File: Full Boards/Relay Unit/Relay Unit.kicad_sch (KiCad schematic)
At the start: 156 parts, among them J3 Program Header, SW1 Status Switch, SW3 SW_MEC_5G, SW4 SW_MEC_5G, U1 ISO1044BD, U10 FM24CL64B-G, U15 LM1117MP-5.0, U2 MAX3232, U3 STM32C092KCT6, U4 ULN2003A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

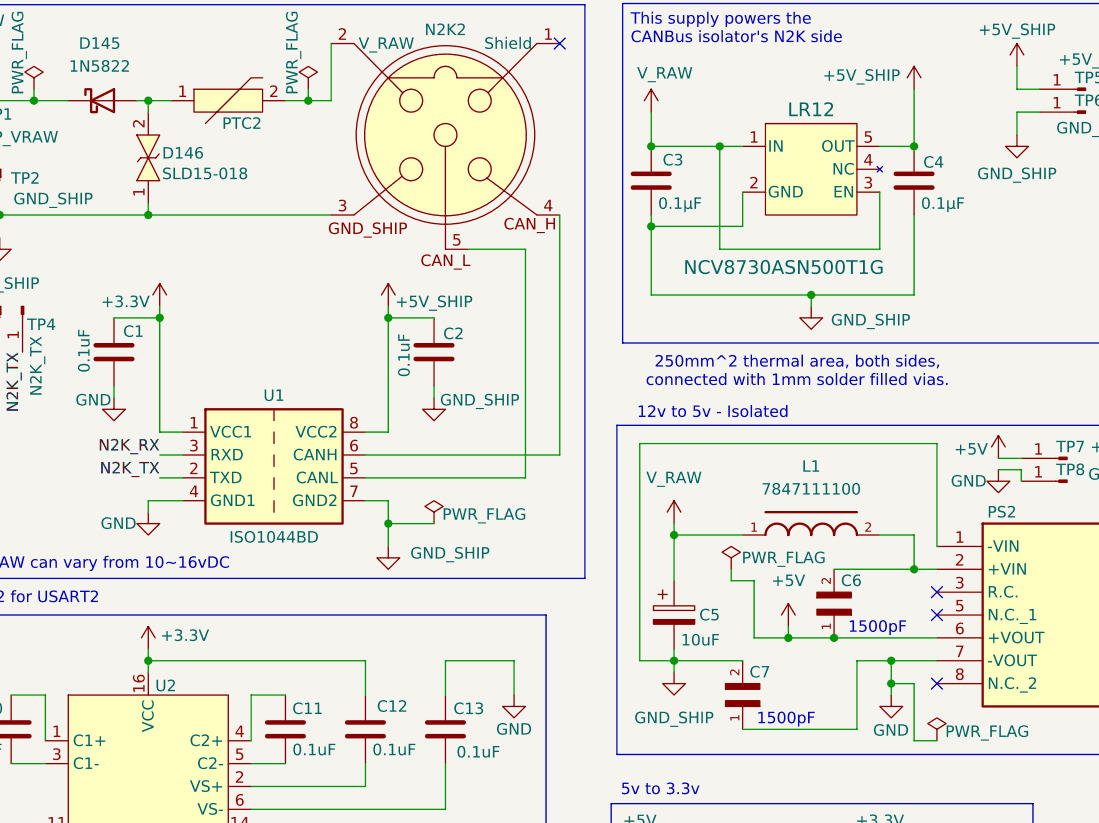
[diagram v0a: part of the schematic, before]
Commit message: Updated PCBs to swap RVS diodes from SLD15-018 to SLD22-018. Also swapped out the inductor from 7847111100 to PA4340.103NLT.
Signed-off-by: Madison Kelly <digital.mermaid@gmail.com>
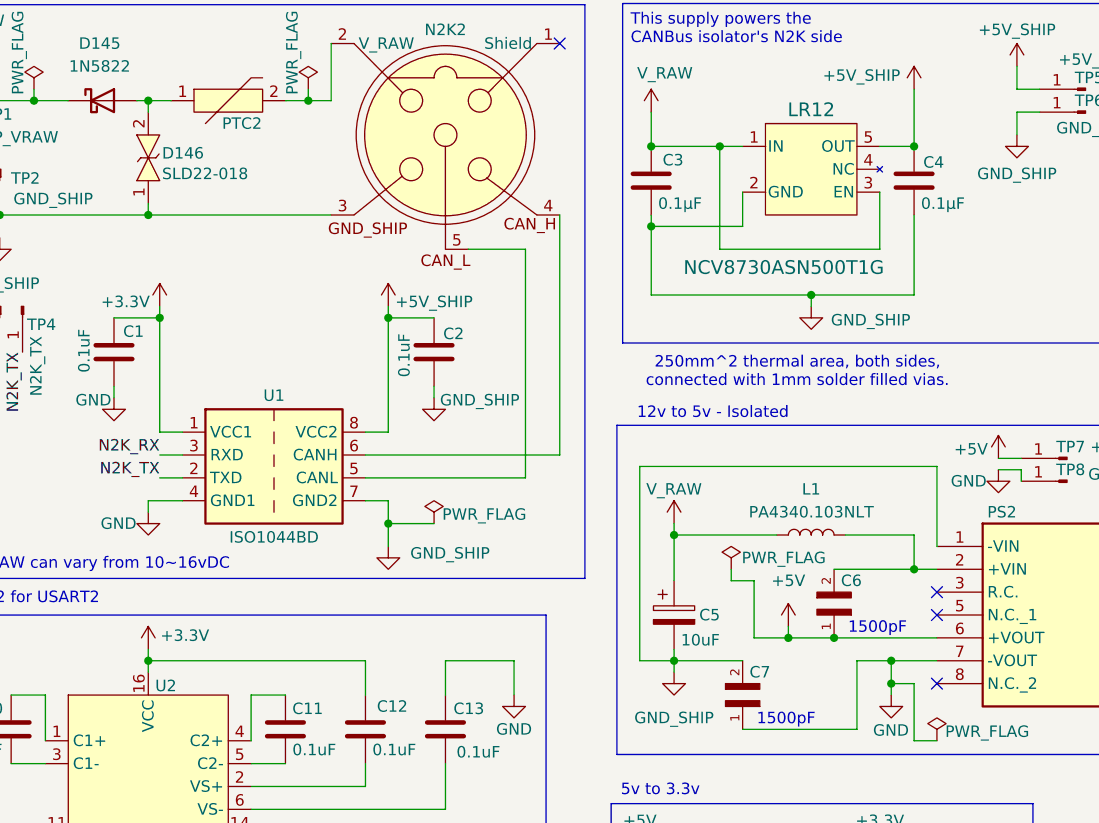
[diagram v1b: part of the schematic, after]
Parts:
- removed L1: 7847111100, mr-stuff:WE-RCIT_7847111100, symbol mr-parts:WE-RCIT
- added L1: PA4340.103NLT, mr-stuff:Pulse PA4340.103NLT, symbol Device:L
- D146: value SLD15-018 -> SLD22-018
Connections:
- net V_RAW: now also L1.1
- net at C6.2, PS2.2 (+VIN): now also L1.2
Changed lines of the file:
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@@
 	(wire
 		(pts
-			(xy 121.92 74.93) (xy 118.11 74.93)
-		)
-		(stroke
-			(width 0)
-			(type default)
-		)
-	)
-	(wire
-		(pts
 			(xy 198.12 224.79) (xy 198.12 227.33)
 		)
@@
 	(wire
 		(pts
-			(xy 91.44 64.77) (xy 91.44 88.9)
+			(xy 91.44 67.31) (xy 91.44 88.9)
 		)
 		(stroke
@@
 	(wire
 		(pts
-			(xy 95.25 74.93) (xy 102.87 74.93)
+			(xy 95.25 74.93) (xy 106.68 74.93)
 		)
 		(stroke
@@
 	(wire
 		(pts
-			(xy 124.46 76.2) (xy 124.46 64.77)
+			(xy 124.46 76.2) (xy 124.46 67.31)
 		)
 		(stroke
@@
 	(wire
 		(pts
-			(xy 124.46 64.77) (xy 91.44 64.77)
+			(xy 124.46 67.31) (xy 91.44 67.31)
 		)
 		(stroke
@@
 	(wire
 		(pts
+			(xy 114.3 74.93) (xy 121.92 74.93)
+		)
+		(stroke
+			(width 0)
+			(type default)
+		)
+	)
+	(wire
+		(pts
 			(xy 124.46 161.29) (xy 132.08 161.29)
 		)
@@
 	)
 	(symbol
+		(lib_id "Device:L")
+		(at 110.49 74.93 90)
+		(unit 1)
+		(exclude_from_sim no)
+		(in_bom yes)
+		(on_board yes)
+		(dnp no)
+		(fields_autoplaced yes)
+		(property "Reference" "L1"
+			(at 110.49 69.85 90)
+			(effects
+				(font
+					(size 1.27 1.27)
+				)
+			)
+		)
+		(property "Value" "PA4340.103NLT"
+			(at 110.49 72.39 90)
+			(effects
+				(font
+					(size 1.27 1.27)
+				)
+			)
+		)
+		(property "Footprint" "mr-stuff:Pulse PA4340.103NLT"
+			(at 110.49 74.93 0)
+			(effects
+				(font
+					(size 1.27 1.27)
+				)
+				(hide yes)
+			)
+		)
+		(property "Datasheet" "~"
+			(at 110.49 74.93 0)
+			(effects
+				(font
+					(size 1.27 1.27)
+				)
+				(hide yes)
+			)
+		)
+		(property "Description" "Inductor"
+			(at 110.49 74.93 0)
+			(effects
+				(font
+					(size 1.27 1.27)
+				)
+				(hide yes)
+			)
+		)
+		(pin "2"
+		)
+		(pin "1"
+		)
+		(instances
+			(project "Relay Unit"
+				(path "/cdf85de7-e063-4a45-8f3b-41b7e4c09bb1"
+					(reference "L1")
+					(unit 1)
+				)
+			)
+		)
+	)
+	(symbol
 		(lib_id "mr-parts:Keystone Electronics 7799")
 		(at 304.8 39.37 0)
@@
 			)
 		)
-		(property "Value" "SLD15-018"
+		(property "Value" "SLD22-018"
 			(at 38.354 34.798 90)
 			(effects
@@
 		(on_board yes)
 		(dnp no)
-		(fields_autoplaced yes)
 		(property "Reference" "#PWR075"
 			(at 95.25 77.47 0)
@@
 		)
 		(property "Value" "V_RAW"
-			(at 95.25 68.58 0)
+			(at 95.25 69.85 0)
 			(effects
 				(font
@@
 					(unit 1)
 				)
-			)
-		)
-	)
-	(symbol
-		(lib_id "mr-parts:WE-RCIT")
-		(at 110.49 74.93 0)
-		(unit 1)
-		(exclude_from_sim no)
-		(in_bom yes)
-		(on_board yes)
-		(dnp no)
-		(fields_autoplaced yes)
-		(property "Reference" "L1"
-			(at 110.49 67.31 0)
-			(effects
-				(font
-					(size 1.27 1.27)
-				)
-			)
-		)
-		(property "Value" "7847111100"
-			(at 110.49 69.85 0)
-			(effects
-				(font
-					(size 1.27 1.27)
-				)
-			)
-		)
-		(property "Footprint" "mr-stuff:WE-RCIT_7847111100"
-			(at 110.744 80.01 0)
-			(effects
-				(font
-					(size 1.27 1.27)
-				)
-				(justify bottom)
-				(hide yes)
-			)
-		)
-		(property "Datasheet" "https://www.we-online.com/components/products/datasheet/7847111100.pdf"
-			(at 110.49 74.93 0)
-			(effects
-				(font
-					(size 1.27 1.27)
-				)
-				(hide yes)
-			)
-		)
-		(property "Description" "10uH, 3A, rod-core inductor"
-			(at 110.49 74.93 0)
-			(effects
-				(font
-					(size 1.27 1.27)
-				)
-				(hide yes)
-			)
-		)
-		(pin "2"
-		)
-		(pin "1"
-		)
-		(instances
-			(project "Relay Unit"
-				(path "/cdf85de7-e063-4a45-8f3b-41b7e4c09bb1"
-					(reference "L1")
-					(unit 1)
-				)

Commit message: Updated boards and schematics.
These are the version that have been ordered. Any further changes will be a new version.

Signed-off-by: Madison Kelly <digital.mermaid@gmail.com>
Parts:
- removed C7: TDK FA28NP01H152JNU06, mr-stuff:TDK CAPRB500W50L400T250H550, symbol mr-parts:TDK FA28NP01H152JNU06
- removed D147, D148, D30, D31, D32, D33, D34, D35, D36, D37, D38, D39, D40, D41, D42, D43, D44, D45, D46, D47: 1N5822, Diode_THT:D_DO-41_SOD81_P10.16mm_Horizontal, symbol Diode:1N4001
- added C25, C7: 0.1uF, mr-stuff:RCE5C1H104J2A2H03B, symbol Device:C
- added J1: Future Bond, Connector_PinHeader_2.54mm:PinHeader_1x03_P2.54mm_Vertical, symbol Connector:Conn_01x03_Pin
- added R10, R11: 3.3K, Resistor_THT:R_Axial_DIN0207_L6.3mm_D2.5mm_P7.62mm_Horizontal, symbol Device:R
- R68: value 10 -> 475
- R7: now fitted
- renumbered N2K2 to N2K1
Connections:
- net +3.3V: now also U2.10 (T2IN), R10.1, R11.1
- net BOARD_I2C_SCL: now also R11.2
- net BOARD_I2C_SDA: now also R10.2
- net GND: now also C25.2, C7.2, J1.2 (Pin_2)
- net GND_SHIP: now also C7.1, J1.3 (Pin_3)
- net STATE_CHECK_SW_IN: now also C25.1
- net at N2K1.1: now also J1.1 (Pin_1)
- no-connect marks 31 -> 29
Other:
- moved on the sheet: C23, C24, C3, C4, C5, C6, C8, C9, D145, D146, H5, L1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
